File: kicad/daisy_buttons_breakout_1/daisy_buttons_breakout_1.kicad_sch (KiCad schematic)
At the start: 27 parts, among them J1 Conn_01x07_Pin, SW1 SW_Push, SW10 SW_Push, SW11 SW_Push, SW12 SW_Push, SW13 SW_Push, SW14 SW_Push, SW15 SW_Push, SW16 SW_Push, SW17 SW_Push, SW18 SW_Push, SW19 SW_Push, SW2 SW_Push, SW20 SW_Push, SW3 SW_Push, SW4 SW_Push, SW5 SW_Push, SW6 SW_Push, SW7 SW_Push, SW8 SW_Push, SW9 SW_Push, U1 MCP23017x-x-SO

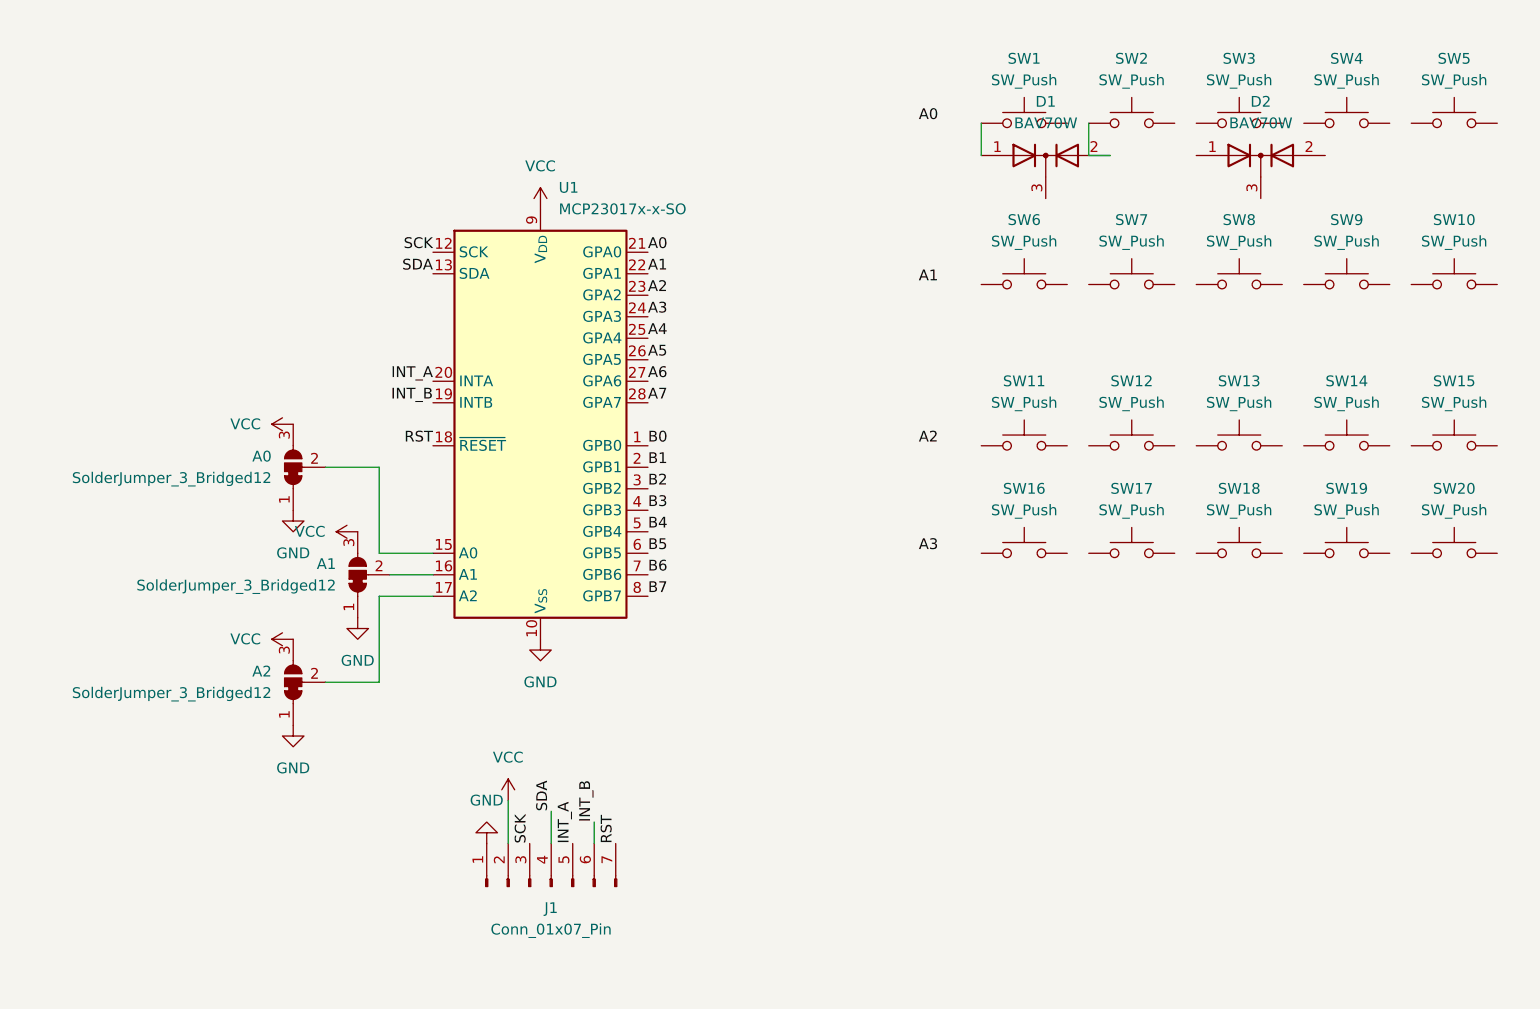
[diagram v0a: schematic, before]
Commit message: Finish carrier PCB for daisy
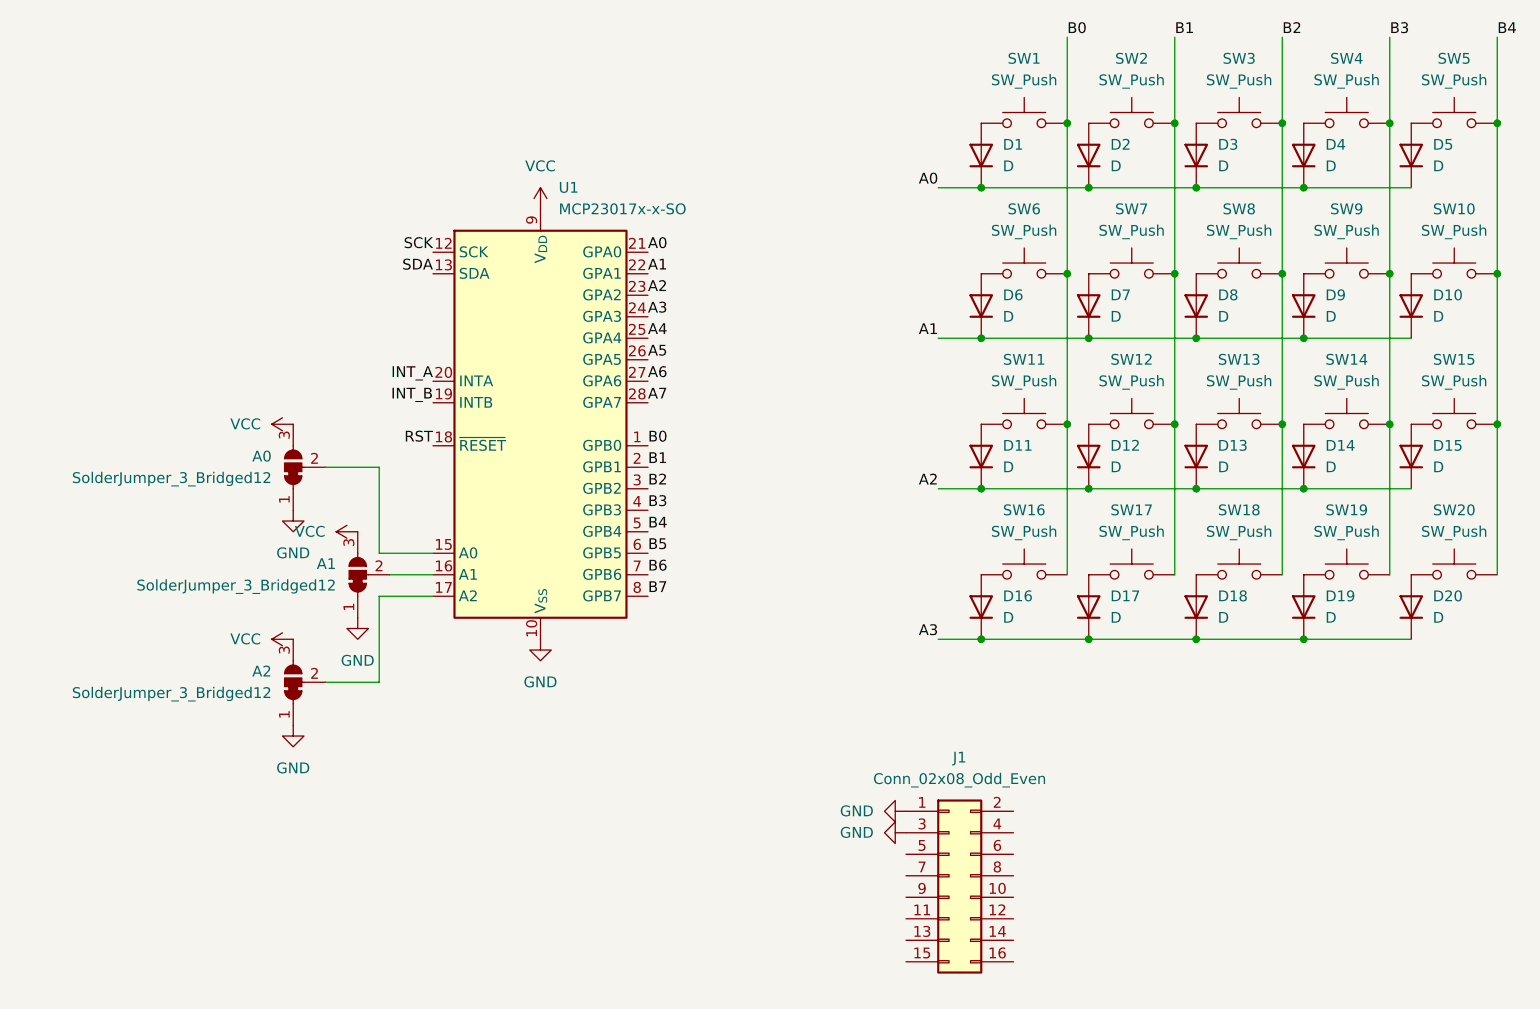
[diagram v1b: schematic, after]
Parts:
- removed D1, D2: BAV70W, Package_TO_SOT_SMD:SOT-323_SC-70, symbol Diode:BAV70W
- removed J1: Conn_01x07_Pin, Connector_PinHeader_2.54mm:PinHeader_1x07_P2.54mm_Vertical, symbol Connector:Conn_01x07_Pin
- added D1, D10, D11, D12, D13, D14, D15, D16, D17, D18, D19, D2, D20, D3, D4, D5, D6, D7, D8, D9: D, Diode_THT:D_DO-35_SOD27_P7.62mm_Horizontal, symbol Device:D
- added J1: Conn_02x08_Odd_Even, Connector_PinSocket_2.54mm:PinSocket_2x08_P2.54mm_Horizontal, symbol Connector_Generic:Conn_02x08_Odd_Even
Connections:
- net A0: now also D1.1 (K), D2.1 (K), D3.1 (K), D4.1 (K), D5.1 (K)
- net A1: now also D10.1 (K), D6.1 (K), D7.1 (K), D8.1 (K), D9.1 (K)
- net A2: now also D11.1 (K), D12.1 (K), D13.1 (K), D14.1 (K), D15.1 (K)
- net A3: now also D16.1 (K), D17.1 (K), D18.1 (K), D19.1 (K), D20.1 (K)
- net B0: now also SW1.2, SW11.2, SW16.2, SW6.2
- net B1: now also SW12.2, SW17.2, SW2.2, SW7.2
- net B2: now also SW13.2, SW18.2, SW3.2, SW8.2
- net B3: now also SW14.2, SW19.2, SW4.2, SW9.2
- net B4: now also SW10.2, SW15.2, SW20.2, SW5.2
- net GND: now also J1.1 (Pin_1), J1.3 (Pin_3)
- net at SW2.1: now also D2.2 (A)
- net at SW20.1: now also D20.2 (A)
- net at SW15.1: now also D15.2 (A)
- net at SW7.1: now also D7.2 (A)
- net at SW5.1: now also D5.2 (A)
- net at SW6.1: now also D6.2 (A)
- net at SW1.1: now also D1.2 (A)
- net at SW18.1: now also D18.2 (A)
- net at SW19.1: now also D19.2 (A)
- net at SW4.1: now also D4.2 (A)
- net at SW16.1: now also D16.2 (A)
- net at SW17.1: now also D17.2 (A)
- net at SW9.1: now also D9.2 (A)
- net at SW11.1: now also D11.2 (A)
- net at SW8.1: now also D8.2 (A)
- net at SW14.1: now also D14.2 (A)
- net at SW13.1: now also D13.2 (A)
- net at SW10.1: now also D10.2 (A)
- net at SW3.1: now also D3.2 (A)
- net at SW12.1: now also D12.2 (A)
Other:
- moved on the sheet: SW10, SW11, SW12, SW13, SW14, SW15, SW16, SW17, SW18, SW19, SW20, SW6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

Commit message: Make side boards for pots and buttons use same connector as main board
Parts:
- added C1: 100nF, Capacitor_SMD:C_0603_1608Metric_Pad1.08x0.95mm_HandSolder, symbol Device:C
- added R1: 10k, Resistor_SMD:R_0603_1608Metric_Pad0.98x0.95mm_HandSolder, symbol Device:R
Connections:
- net GND: now also J1.13 (Pin_13), J1.16 (Pin_16), C1.2
- net INT_A: now also J1.10 (Pin_10)
- net RST: now also J1.11 (Pin_11), R1.2
- net SCK: now also J1.6 (Pin_6)
- net SDA: now also J1.5 (Pin_5)
- net VCC: now also J1.4 (Pin_4), C1.1, R1.1
- no-connect marks 0 -> 7
